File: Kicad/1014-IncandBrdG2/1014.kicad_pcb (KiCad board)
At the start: 2 copper layers, 44.4 x 20.3 mm, 24 parts, among them P1 TST, P2 CONN_4, P3 CONN_4, P4 SPADE_187, P5 CONN_8, P6 CONN_2, P7 CONN_8, Q1 MOSFET_N, Q2 MOSFET_N, Q3 MOSFET_N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

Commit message: Updates to silkscreen and created mashup.  These Gerbers sent to PCB house.
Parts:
- R1: value 100K -> 0
- moved P6 1.91 mm to (166.4, 151.8)
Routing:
- net +12V1: track 81.7 -> 82.2 mm
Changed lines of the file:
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@@
     (links 50)
     (no_connects 0)
-    (area 163.754999 140.894999 208.355001 161.365001)
+    (area 162.754734 140.529734 208.686401 161.696401)
     (thickness 1.6)
     (drawings 7)
@@
   )
   (setup
-    (last_trace_width 0.4826)
+    (last_trace_width 0.254)
     (user_trace_width 0.4826)
-    (user_trace_width 1.27)
+    (user_trace_width 1.143)
     (trace_clearance 0.254)
     (zone_clearance 0.254)
@@
   )
   (module 00_th1x2x4.2mm_nopeg (layer F.Cu)
-    (at 166.37 153.67)
+    (at 166.37 151.765)
     (descr "Double rangee de contacts 2 x 8 pins")
     (tags CONN)
-    (fp_text reference P6 (at 1.905 -5.715) (layer F.SilkS)
+    (fp_text reference P6 (at 3.81 -4.445) (layer F.SilkS)
       (effects (font (size 1.016 1.016) (thickness 0.2032)))
     )
@@
     (tags R)
     (autoplace_cost180 10)
-    (fp_text reference R1 (at 0 -1.905 180) (layer F.SilkS)
+    (fp_text reference R1 (at 3.81 -1.27 180) (layer F.SilkS)
       (effects (font (size 0.762 0.762) (thickness 0.1524)))
     )
-    (fp_text value 100K (at 0 0.127 180) (layer F.SilkS)
+    (fp_text value 0 (at 0 0.127 180) (layer F.SilkS)
       (effects (font (size 1.397 1.27) (thickness 0.2032)))
     )
@@
     )
   )
-  (gr_text Gnd (at 174.752 144.272) (layer F.SilkS)
+  (gr_text Gnd (at 175.895 157.48 90) (layer F.SilkS)
     (effects (font (size 0.762 0.762) (thickness 0.1524)))
   )
-  (gr_text 5V (at 171.704 144.272) (layer F.SilkS)
+  (gr_text 5V (at 169.799 157.861 90) (layer F.SilkS)
     (effects (font (size 0.762 0.762) (thickness 0.1524)))
   )
-  (gr_text 12V (at 169.672 144.272) (layer F.SilkS)
+  (gr_text 12V (at 168.529 157.607 90) (layer F.SilkS)
     (effects (font (size 0.762 0.762) (thickness 0.1524)))
   )
@@
   (gr_line (start 163.83 161.29) (end 208.28 161.29) (angle 90) (layer Edge.Cuts) (width 0.15))
   (gr_line (start 163.83 140.97) (end 163.83 161.29) (angle 90) (layer Edge.Cuts) (width 0.15))
+  (segment (start 168.91 142.24) (end 168.91 143.51) (width 1.143) (layer F.Cu) (net 1))
+  (segment (start 168.275 159.385) (end 168.91 160.02) (width 1.143) (layer F.Cu) (net 1))
+  (segment (start 168.275 144.145) (end 168.275 159.385) (width 1.143) (layer F.Cu) (net 1))
+  (segment (start 168.91 143.51) (end 168.275 144.145) (width 1.143) (layer F.Cu) (net 1))
   (segment (start 168.91 142.24) (end 169.545 142.24) (width 0.4826) (layer B.Cu) (net 1))
   (segment (start 184.785 143.51) (end 186.69 145.415) (width 0.4826) (layer B.Cu) (net 1))
   (segment (start 170.815 143.51) (end 184.785 143.51) (width 0.4826) (layer B.Cu) (net 1))
   (segment (start 169.545 142.24) (end 170.815 143.51) (width 0.4826) (layer B.Cu) (net 1))
-  (segment (start 168.91 142.24) (end 168.91 160.02) (width 0.508) (layer F.Cu) (net 1))
   (segment (start 186.69 154.305) (end 186.69 156.845) (width 0.635) (layer B.Cu) (net 1))
   (segment (start 186.69 156.845) (end 184.785 158.75) (width 0.635) (layer B.Cu) (net 1))
@@
   (segment (start 197.485 145.415) (end 197.485 147.955) (width 0.635) (layer B.Cu) (net 1))
   (segment (start 197.485 147.955) (end 195.58 149.86) (width 0.635) (layer B.Cu) (net 1))
-  (segment (start 171.45 142.24) (end 170.18 143.51) (width 0.508) (layer F.Cu) (net 2))
-  (segment (start 170.18 158.75) (end 171.45 160.02) (width 0.508) (layer F.Cu) (net 2))
-  (segment (start 170.18 143.51) (end 170.18 158.75) (width 0.508) (layer F.Cu) (net 2))
+  (segment (start 171.45 142.24) (end 171.45 143.51) (width 1.143) (layer F.Cu) (net 2))
+  (segment (start 169.672002 158.242002) (end 171.45 160.02) (width 1.143) (layer F.Cu) (net 2))
+  (segment (start 169.672002 145.287998) (end 169.672002 158.242002) (width 1.143) (layer F.Cu) (net 2))
+  (segment (start 171.45 143.51) (end 169.672002 145.287998) (width 1.143) (layer F.Cu) (net 2))
   (segment (start 191.135 144.145) (end 189.865 142.875) (width 0.254) (layer F.Cu) (net 3))
   (segment (start 189.865 142.875) (end 186.69 142.875) (width 0.254) (layer F.Cu) (net 3))
@@
   (segment (start 203.835 157.48) (end 201.93 157.48) (width 0.254) (layer F.Cu) (net 10))
   (segment (start 206.375 160.02) (end 203.835 157.48) (width 0.254) (layer F.Cu) (net 10))
-  (segment (start 173.99 143.51) (end 172.72 144.78) (width 0.4826) (layer F.Cu) (net 11) (status 800000))
-  (segment (start 173.99 142.24) (end 173.99 143.51) (width 0.635) (layer F.Cu) (net 11))
-  (segment (start 173.99 159.385) (end 173.99 160.02) (width 0.635) (layer F.Cu) (net 11))
-  (segment (start 176.53 156.845) (end 173.99 159.385) (width 0.635) (layer F.Cu) (net 11))
-  (segment (start 176.53 154.305) (end 176.53 156.845) (width 0.635) (layer F.Cu) (net 11))
-  (segment (start 175.26 153.035) (end 176.53 154.305) (width 0.635) (layer F.Cu) (net 11))
-  (segment (start 175.26 144.78) (end 175.26 147.32) (width 0.635) (layer F.Cu) (net 11))
-  (segment (start 175.26 147.32) (end 175.26 153.035) (width 0.635) (layer F.Cu) (net 11))
-  (segment (start 173.99 143.51) (end 175.26 144.78) (width 0.635) (layer F.Cu) (net 11))
+  (segment (start 173.99 143.51) (end 172.72 144.78) (width 1.27) (layer F.Cu) (net 11))
+  (segment (start 173.99 160.02) (end 176.53 157.48) (width 1.27) (layer F.Cu) (net 11))
+  (segment (start 173.99 143.51) (end 173.99 142.24) (width 1.27) (layer F.Cu) (net 11))
+  (segment (start 176.53 146.05) (end 173.99 143.51) (width 1.27) (layer F.Cu) (net 11))
+  (segment (start 176.53 157.48) (end 176.53 146.05) (width 1.27) (layer F.Cu) (net 11))
   (segment (start 179.705 147.32) (end 182.88 147.32) (width 0.254) (layer F.Cu) (net 13))
   (segment (start 182.88 147.32) (end 184.15 148.59) (width 0.254) (layer F.Cu) (net 13))

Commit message: Added OPP logo to all boards.  Better late than never.
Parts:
- added VAL: REF, opp_logo_backsilk, F.Cu at (176.5, 149.2)

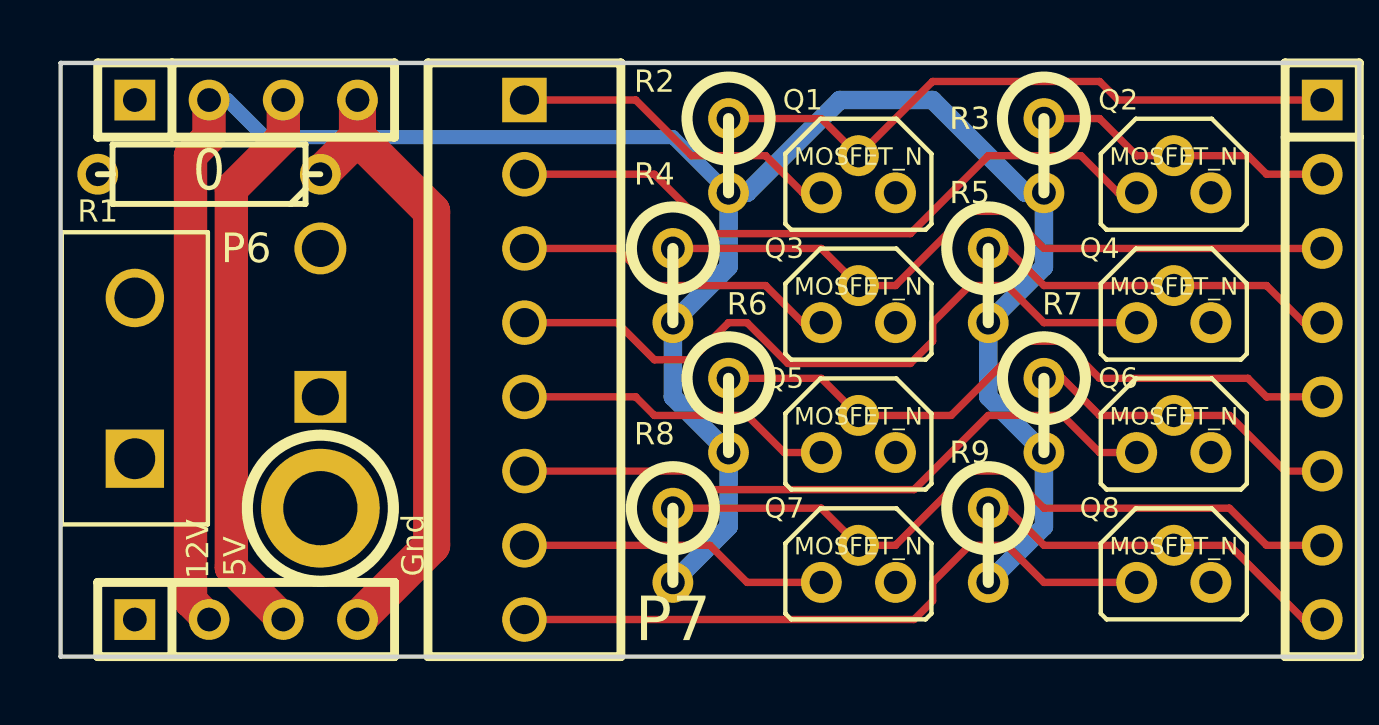
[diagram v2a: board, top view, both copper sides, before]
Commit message: Fix labeling issue on the incandescent board.
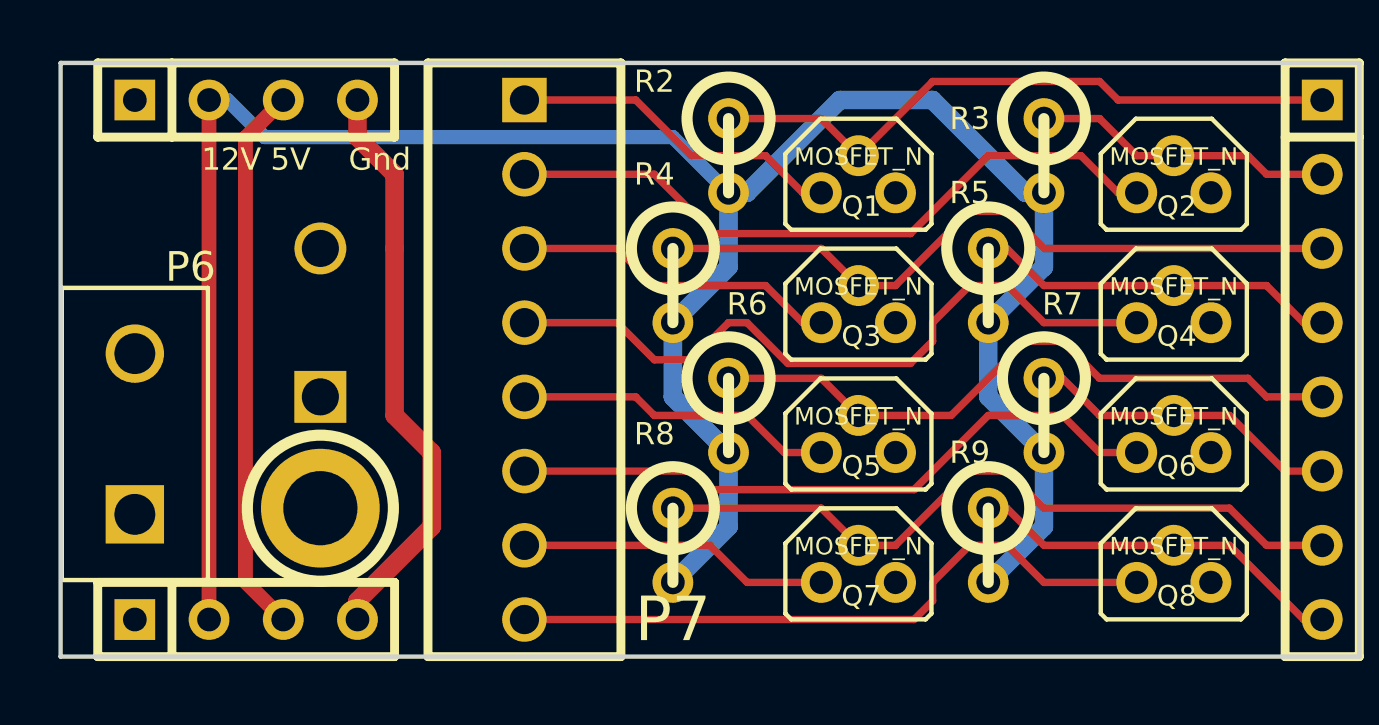
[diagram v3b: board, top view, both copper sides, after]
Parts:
- removed R1: 0, R3
- Q1, Q2, Q3, Q4, Q5, Q6, Q7, Q8: footprint 00_to92_dgs -> 00_to92_sgd
- moved P6 1.91 mm to (166.4, 153.7)
- moved VAL 0.64 mm to (176.5, 149.9)
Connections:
- P2 pad 1: GNDPWR -> +VLED
- P3 pad 1: GNDPWR -> +VLED
- P4 pad 1: GNDPWR -> +VLED
- P4 pad 2: GNDPWR -> +VLED
- P6 pad 1: GNDPWR -> +VLED
- P6 pad 2: GNDPWR -> +VLED
- P7 pad 1: N-000008 -> N-000003
- P7 pad 2: N-000009 -> N-000004
- P7 pad 3: N-0000010 -> N-000002
- P7 pad 4: N-000002 -> N-000005
- P7 pad 5: N-000003 -> N-000006
- P7 pad 6: N-000004 -> N-000007
- P7 pad 7: N-000005 -> N-000008
- P7 pad 8: N-000006 -> N-000009
- Q1 pad D: N-000008 -> +VLED
- Q1 pad S: GNDPWR -> N-000003
- Q2 pad D: N-000009 -> +VLED
- Q2 pad S: GNDPWR -> N-000004
- Q3 pad D: N-0000010 -> +VLED
- Q3 pad S: GNDPWR -> N-000002
- Q4 pad D: N-000002 -> +VLED
- Q4 pad S: GNDPWR -> N-000005
- Q5 pad D: N-000003 -> +VLED
- Q5 pad S: GNDPWR -> N-000006
- Q6 pad D: N-000004 -> +VLED
- Q6 pad S: GNDPWR -> N-000007
- Q7 pad D: N-000005 -> +VLED
- Q7 pad S: GNDPWR -> N-000008
- Q8 pad D: N-000006 -> +VLED
- Q8 pad S: GNDPWR -> N-000009
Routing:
- net N-000007: track 0.00 -> 22.8 mm
- net N-000005: track 10.7 -> 24.6 mm
- net N-000002: track 24.6 -> 11.2 mm
- net N-000006: track 22.9 -> 10.9 mm
- net N-0000010: track 11.2 -> 0.00 mm
- net GND: track 21.7 -> 19.9 mm
- net N-000008: track 11.5 -> 10.7 mm
- net N-000004: track 22.8 -> 23.4 mm
- net N-000003: track 10.9 -> 11.5 mm
- net +12V1: track 82.2 -> 81.7 mm
- net N-000009: track 23.4 -> 22.9 mm
- added copper zone on B.Cu, net +VLED
- removed copper zone on B.Cu, net GNDPWR

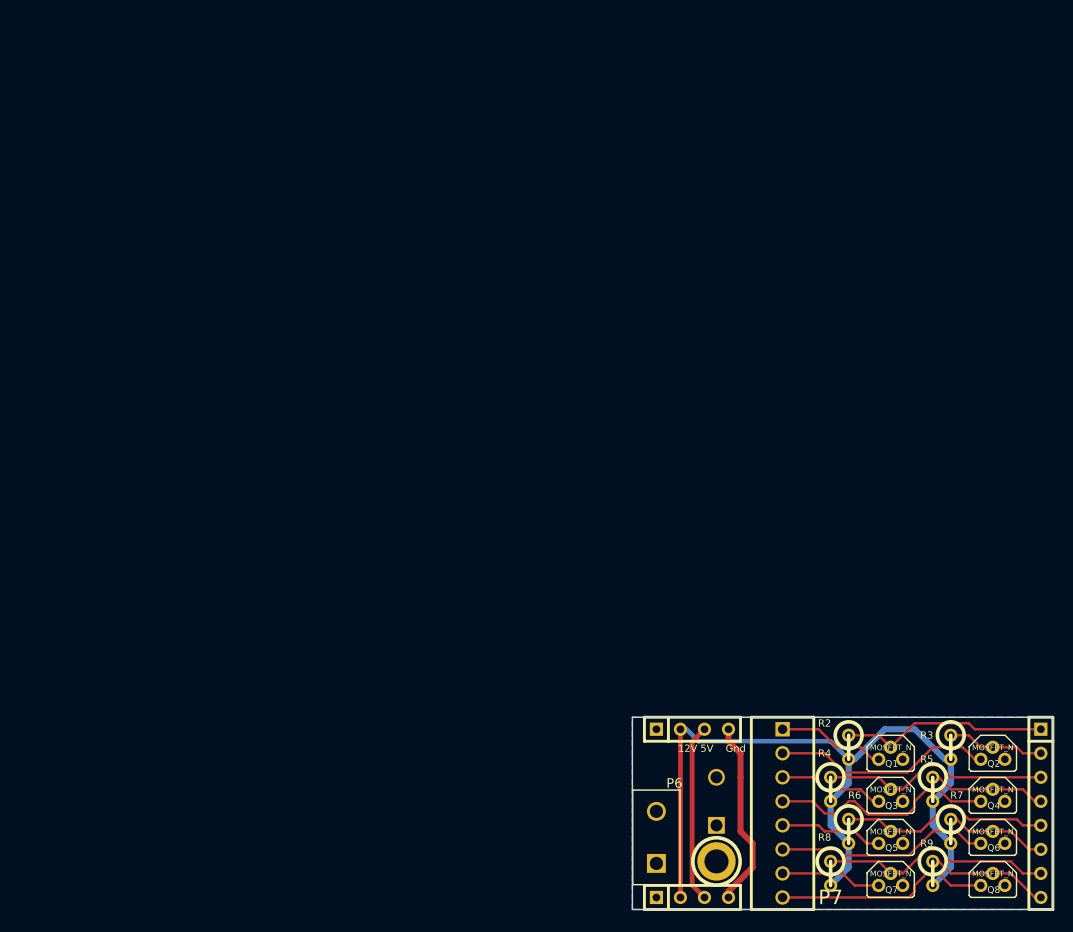
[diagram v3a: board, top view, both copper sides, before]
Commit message: Changed size of PCB sheets to 8.5" x 11".  Added name/rev/board name to PCB sheets.
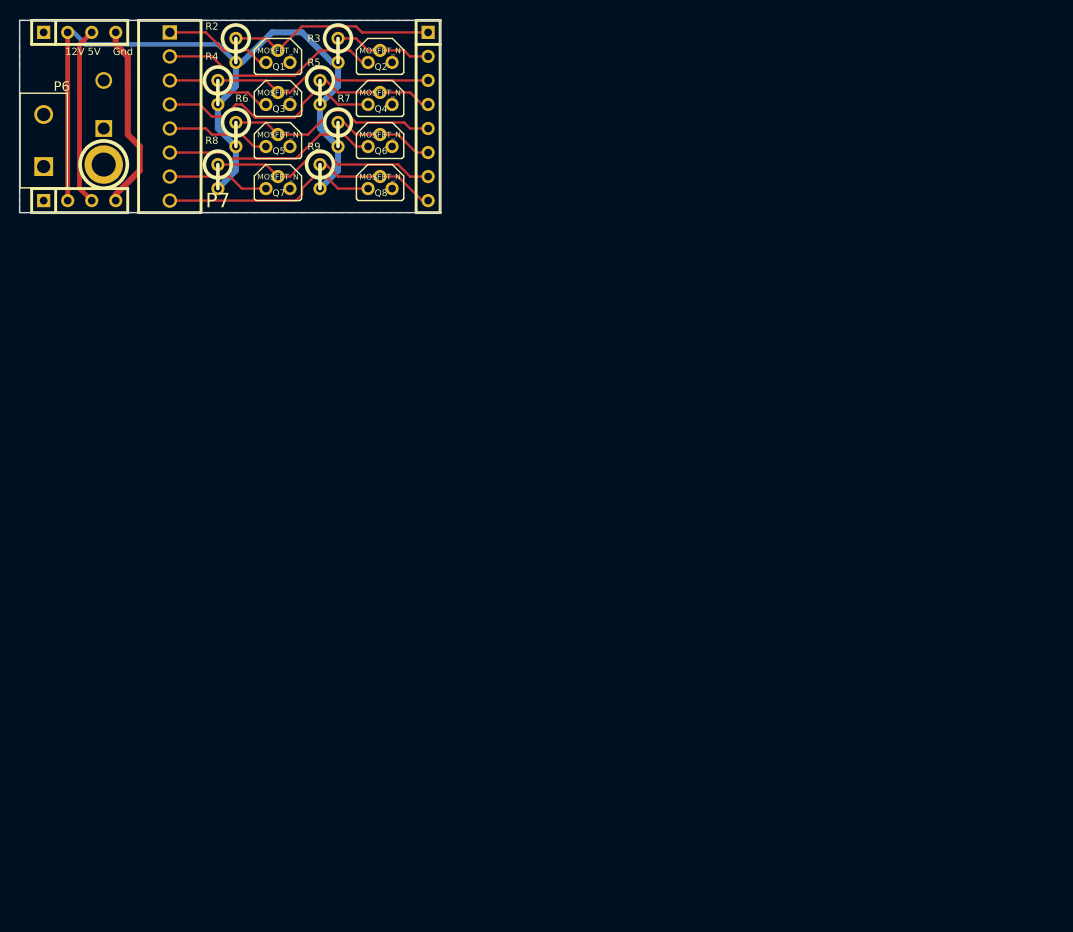
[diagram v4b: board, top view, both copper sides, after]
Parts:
- moved P1 98.1 mm to (108.0, 82.5)
- moved P2 98.1 mm to (105.4, 68.6)
- moved P3 98.1 mm to (105.4, 86.4)
- moved P4 98.1 mm to (108.0, 76.2)
- moved P7 98.1 mm to (114.9, 77.5)
- moved Q2 98.1 mm to (137.2, 71.1)
- moved Q4 98.1 mm to (137.2, 75.6)
- moved Q7 98.1 mm to (126.4, 84.5)
- moved Q8 98.1 mm to (137.2, 84.5)
- moved R2 98.1 mm to (121.9, 70.5)
- moved R3 98.1 mm to (132.7, 70.5)
- moved R5 98.1 mm to (130.8, 74.9)
- moved R7 98.1 mm to (132.7, 79.4)
- moved R9 98.1 mm to (130.8, 83.8)
- moved VAL 98.1 mm to (111.8, 76.2)
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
